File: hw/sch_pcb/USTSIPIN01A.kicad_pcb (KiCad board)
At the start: 2 copper layers, 90.9 x 50.3 mm, 112 parts, among them J1 HEADER_2x01_PARALLEL, J19 HEADER_2x01_PARALLEL, J2 HEADER_2x01_PARALLEL, J22 HEADER_2x03, J3 HEADER_2x01_PARALLEL, J4 HEADER_1x01, J5 HEADER_1x01, J6 HEADER_1x01, J7 HEADER_1x01, M1 HOLE, M2 HOLE, M3 HOLE, M4 HOLE, M5 BMI-S-210-F, M6 BMI-S-210-F, M7 BMI-S-210-F, M8 BMI-S-204-F, U1 OPA2314, U10 ATMEGA1284P-AU, U11 PCF85263A, U2 OPA2314, U3 ISL21080DIH312Z-TK 1V25, U4 TS7211, U5 TS5A4594, U6 TPS613221ADBV, U8 TPS613222ADBV, Y1 16MHz, Y2 ABS07-120-32.768KHZ-T

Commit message: Edit schema
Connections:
- C24 pad 1: /K -> /Ubiasout
- R22 pad 1: /K -> /Ubiasout
- U10 pad 11: (no net) -> unconnected-(U10-Pad11)
- U10 pad 12: (no net) -> unconnected-(U10-Pad12)
- U10 pad 13: (no net) -> unconnected-(U10-Pad13)
- U10 pad 14: (no net) -> unconnected-(U10-Pad14)
- U10 pad 15: (no net) -> unconnected-(U10-Pad15)
- U10 pad 16: (no net) -> unconnected-(U10-Pad16)
- U10 pad 21: (no net) -> unconnected-(U10-Pad21)
- U10 pad 23: (no net) -> unconnected-(U10-Pad23)
- U10 pad 24: (no net) -> unconnected-(U10-Pad24)
- U10 pad 25: (no net) -> unconnected-(U10-Pad25)
- U10 pad 30: (no net) -> unconnected-(U10-Pad30)
- U10 pad 31: (no net) -> unconnected-(U10-Pad31)
- U10 pad 32: (no net) -> unconnected-(U10-Pad32)
- U10 pad 33: (no net) -> unconnected-(U10-Pad33)
- U10 pad 34: (no net) -> unconnected-(U10-Pad34)
- U10 pad 35: (no net) -> unconnected-(U10-Pad35)
- U10 pad 41: (no net) -> unconnected-(U10-Pad41)
- U10 pad 42: (no net) -> unconnected-(U10-Pad42)
- U10 pad 43: (no net) -> unconnected-(U10-Pad43)
- U10 pad 44: (no net) -> unconnected-(U10-Pad44)
- U11 pad 4: (no net) -> unconnected-(U11-Pad4)
- U11 pad 8: (no net) -> unconnected-(U11-Pad8)
- U11 pad 9: (no net) -> unconnected-(U11-Pad9)
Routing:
- net /Ubiasout: track 0.00 -> 5.94 mm
- net /K: track 5.94 -> 0.00 mm

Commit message: Edit schema
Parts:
- added C22: 10uF, Mlab_R:SMD-0805, F.Cu at (68.6, 20.3)
- added C25: 100nF, Mlab_R:SMD-0805, F.Cu at (72.8, 20.3)
- added C36: 100nF, Mlab_R:SMD-0805, F.Cu at (81.6, 12.9)
- added C37: 1uF, Mlab_R:SMD-0805, F.Cu at (34.5, 54.9)
- added C38: 10uF, Mlab_C:SMD-0805, F.Cu at (133.4, 9.87)
- added C41: 10uF, Mlab_C:SMD-0805, F.Cu at (114.5, 27.0)
- added C45: 100nF, Mlab_C:SMD-0805, F.Cu at (121.0, 20.2)
- added C46: 100nF, Mlab_C:SMD-0805, F.Cu at (106.2, 36.6)
- added C48: 100nF, Mlab_C:SMD-0805, F.Cu at (120.7, 23.0)
- added D1: BZX585-B5V6.115, Diode_SMD:D_SOD-523, F.Cu at (108.0, 26.6)
- added D3: RED, Mlab_D:LED_1206, F.Cu at (128.2, 9.77)
- added D4: GREEN, Mlab_D:LED_1206, F.Cu at (115.5, 23.7)
- added J1: SM08B-GHS-TB, Connector_JST:JST_GH_SM08B-GHS-TB_1x08-1MP_P1.25mm_Horizontal, F.Cu at (74.2, 7.81)
- added J10: HEADER_2x01_PARALLEL, Mlab_Pin_Headers:Straight_2x01, F.Cu at (109.3, 29.8)
- added J11: HEADER_2x01_PARALLEL, Mlab_Pin_Headers:Straight_2x01, F.Cu at (128.2, 5.93)
- added J12: HEADER_2x01_PARALLEL, Mlab_Pin_Headers:Straight_2x01, F.Cu at (122.0, 9.62)
- added J13: -, Mlab_Pin_Headers:Straight_2x01, F.Cu at (122.0, 17.0)
- added J14: -, Mlab_Pin_Headers:Straight_2x01, F.Cu at (103.1, 29.8)
- added J15: -, Mlab_Pin_Headers:Straight_2x01, F.Cu at (103.1, 33.5)
- added J16: -, Mlab_Pin_Headers:Straight_2x01, F.Cu at (109.3, 23.5)
- added J17: HEADER_2x01_PARALLEL, Mlab_Pin_Headers:Straight_2x01, F.Cu at (122.0, 13.3)
- added J18: -, Mlab_Pin_Headers:Straight_1x01, F.Cu at (118.4, 27.5)
- added J2: SD_Card-FPS009-4200-0, Mlab_CON:FPS009-4200-0, F.Cu at (65.7, 24.6)
- added J20: -, Mlab_Pin_Headers:Straight_1x01, F.Cu at (124.9, 20.7)
- added J21: -, Mlab_Pin_Headers:Straight_1x01, F.Cu at (112.2, 33.5)
- added J23: -, Mlab_Pin_Headers:Straight_1x01, F.Cu at (131.1, 13.6)
- added J3: SM06B-GHS-TB, Connector_JST:JST_GH_SM06B-GHS-TB_1x06-1MP_P1.25mm_Horizontal, F.Cu at (73.0, 15.3)
- added J4: HEADER_1x01, Mlab_Pin_Headers:Straight_1x01, F.Cu at (68.3, 23.5)
- added J5: HEADER_1x01, Mlab_Pin_Headers:Straight_1x01, F.Cu at (46.3, 43.4)
- added J6: HEADER_1x01, Mlab_Pin_Headers:Straight_1x01, F.Cu at (50.0, 43.4)
- added J7: HEADER_1x01, Mlab_Pin_Headers:Straight_1x01, F.Cu at (42.6, 43.4)
- added J8: USB_B, Connector_USB:USB_B_OST_USB-B1HSxx_Horizontal, F.Cu at (102.8, 11.6)
- added J9: HEADER_2x01_PARALLEL, Mlab_Pin_Headers:Straight_2x01, F.Cu at (122.0, 5.93)
- added L2: L, Mlab_R:SMD-0805, F.Cu at (30.3, 45.6)
- added Q1: BF862, Mlab_T:SOT-23, F.Cu at (30.1, 53.0)
- added R14: 4k7, Mlab_R:SMD-0805, F.Cu at (34.1, 52.2)
- added R16: 4k7, Mlab_R:SMD-0805, F.Cu at (30.3, 56.4)
- added R17: 100, Mlab_R:SMD-0805, F.Cu at (34.5, 45.6)
- added R18: 100, Mlab_R:SMD-0805, F.Cu at (38.7, 42.9)
- added R24: 100, Mlab_R:SMD-0805, F.Cu at (34.5, 42.9)
- added R25: 100, Mlab_R:SMD-0805, F.Cu at (30.3, 42.9)
- added R26: 4k7, Mlab_R:SMD-0805, F.Cu at (108.3, 33.0)
- added R27: 10k, Mlab_R:SMD-0805, F.Cu at (127.2, 15.8)
- added R28: 270R, Mlab_R:SMD-0805, F.Cu at (127.2, 13.1)
- added R29: 270R, Mlab_R:SMD-0805, F.Cu at (102.0, 36.6)
- added U6: AT24CS64-SSHM, Package_SO:SOIC-8_3.9x4.9mm_P1.27mm, F.Cu at (86.2, 7.31)
- added U7: USBLC6-2SC6, Package_TO_SOT_SMD:SOT-23-6, F.Cu at (133.9, 6.31)
- added U9: FT231XQ, Package_DFN_QFN:QFN-20-1EP_4x4mm_P0.5mm_EP2.5x2.5mm, F.Cu at (103.1, 24.8)
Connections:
- C1 pad 1: +3V3 -> POWER_ANALOG_3V3
- C32 pad 1: VDD -> POWER_ANALOG_3V3
- C4 pad 1: +3V3 -> POWER_ANALOG_3V3
- F2 pad 2: /power/3 -> UAV_5V
- L3 pad 1: VDD -> POWER_ANALOG_3V3
- R2 pad 2: +3V3 -> POWER_ANALOG_3V3
- R3 pad 2: +3V3 -> POWER_ANALOG_3V3
- R4 pad 2: +3V3 -> POWER_ANALOG_3V3
- R5 pad 2: +3V3 -> POWER_ANALOG_3V3
- U10 pad 11: unconnected-(U10-Pad11) -> /cpu/RX1
- U10 pad 12: unconnected-(U10-Pad12) -> /cpu/TX1
- U10 pad 13: unconnected-(U10-Pad13) -> /cpu/TIMEPULSE
- U10 pad 14: unconnected-(U10-Pad14) -> /cpu/EXTINT
- U10 pad 15: unconnected-(U10-Pad15) -> /cpu/GEO_STAT
- U10 pad 16: unconnected-(U10-Pad16) -> POWER_ANALOG_3V3
- U10 pad 23: unconnected-(U10-Pad23) -> /cpu/PC4
- U10 pad 26: /cpu/PC7 -> unconnected-(U10-Pad26)
- U10 pad 41: unconnected-(U10-Pad41) -> Net-(L2-Pad1)
- U10 pad 42: unconnected-(U10-Pad42) -> Net-(L2-Pad1)
- U10 pad 43: unconnected-(U10-Pad43) -> Net-(L2-Pad1)
- U10 pad 44: unconnected-(U10-Pad44) -> /cpu/PB4
- U3 pad 1: +3V3 -> POWER_ANALOG_3V3
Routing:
- net unconnected-(U10-Pad26): track 0.00 -> 20.3 mm
- net /cpu/PC7: track 20.3 -> 0.00 mm

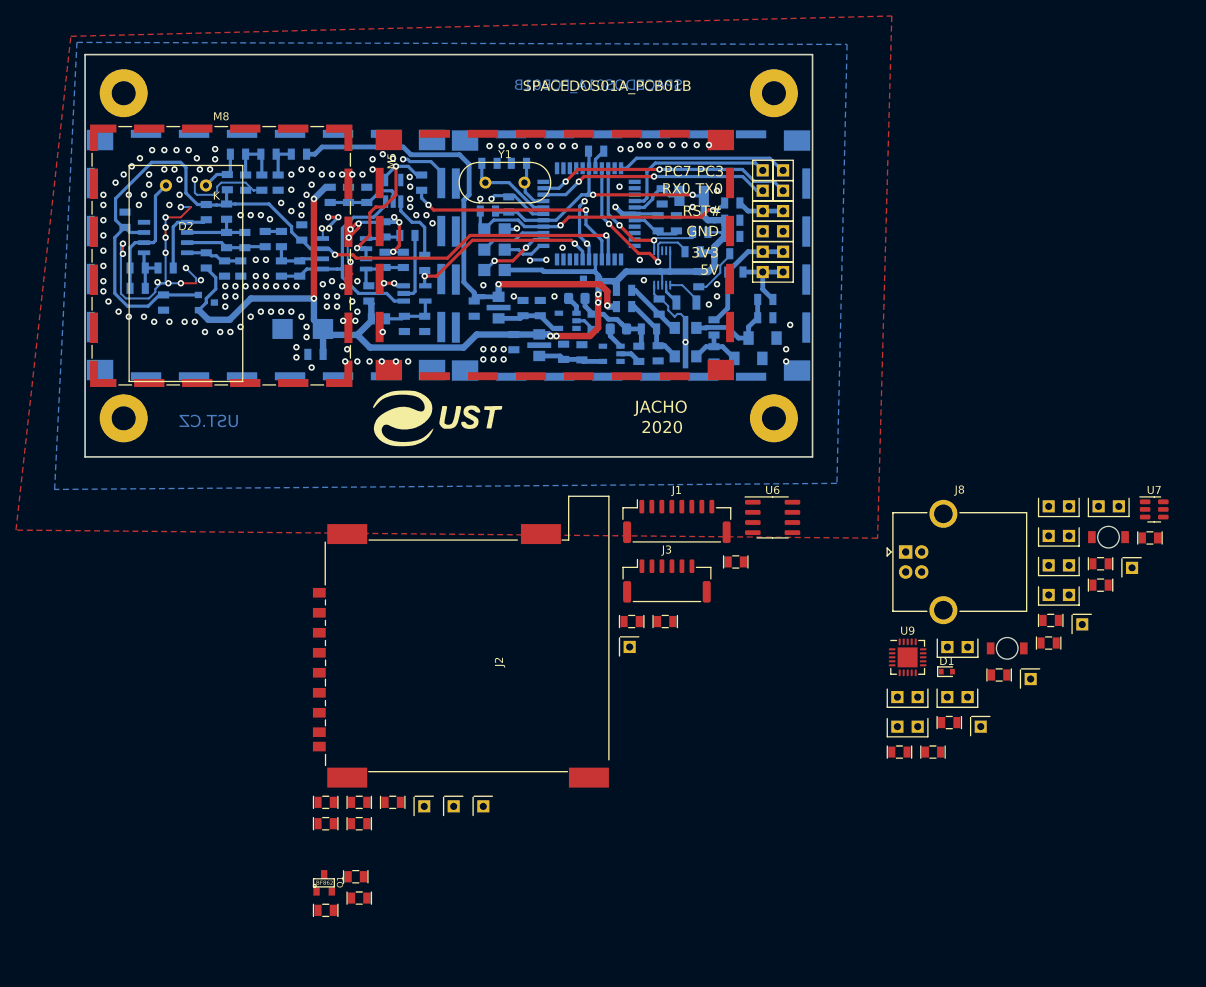
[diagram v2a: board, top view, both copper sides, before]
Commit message: Edit schema and PCB
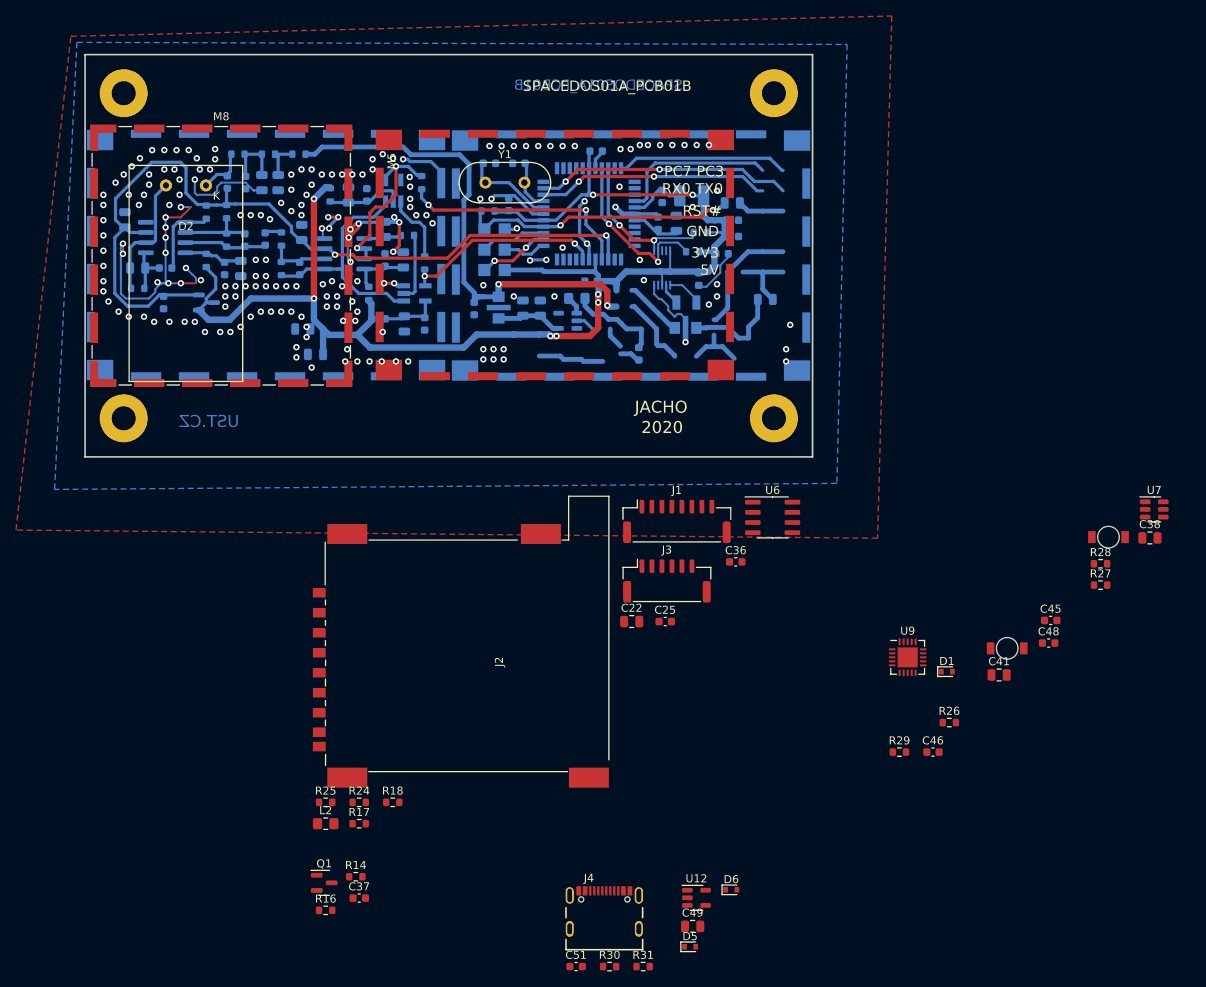
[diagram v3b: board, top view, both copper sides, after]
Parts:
- removed the C22 at (78.9, -13.1)
- removed the C25 at (63.8, -17.1)
- removed the C36 at (85.3, -17.7)
- removed the C38 at (60.1, -13.4)
- removed the C45 at (75.3, -12.8)
- removed the C48 at (71.9, -13.2)
- removed C53, C55: 100nF, Mlab_R:SMD-0805
- removed the D1 at (83.2, -12.6)
- removed the D3 at (84.9, -15.1)
- removed F1: SR010-15 100mA, Mlab_R:SMD-0805
- removed G***: LOGO, MLAB_LOGA:UST
- removed the J1 at (86.2, -25.9)
- removed J10, J11, J12, J17, J19, J9: HEADER_2x01_PARALLEL, Mlab_Pin_Headers:Straight_2x01
- removed J13, J14, J15, J16: -, Mlab_Pin_Headers:Straight_2x01
- removed J18, J20, J21, J23: -, Mlab_Pin_Headers:Straight_1x01
- removed the J2 at (86.2, -28.4)
- removed the J3 at (86.2, -23.4)
- removed the J4 at (85.0, -36.1)
- removed the J4 at (68.3, 23.5)
- removed J5 (x2), J6 (x2), J7 (x2): HEADER_1x01, Mlab_Pin_Headers:Straight_1x01
- removed J8: USB_B, Connector_USB:USB_B_OST_USB-B1HSxx_Horizontal
- removed the L2 at (66.9, -16.3)
- removed the R24 at (81.5, -23.4)
- removed the R25 at (67.6, -19.1)
- removed the R27 at (67.6, -21.1)
- removed the R28 at (70.7, -16.3)
- removed the U6 at (66.1, -13.1)
- added D5: BZX585-B5V6.115, Diode_SMD:D_SOD-523, F.Cu at (75.9, 61.0)
- added D6: BZX585-B5V6.115, Diode_SMD:D_SOD-523, F.Cu at (81.0, 53.9)
- added J4: USBC_USB4105-GF-A, Mlab_CON:USBC GCT_USB4105-GF-A, F.Cu at (65.2, 58.7)
- added R30: 5k1, Resistor_SMD:R_0603_1608Metric, F.Cu at (65.8, 63.5)
- added R31: 5k1, Resistor_SMD:R_0603_1608Metric, F.Cu at (70.0, 63.5)
- added U12: MIC5504-3.3YM5, Package_TO_SOT_SMD:SOT-23-5, F.Cu at (76.7, 54.9)
- C1: value 47uF -> 47uF/6V3; footprint Mlab_C:TantalC_SizeC_Reflow -> Capacitor_SMD:C_0805_2012Metric
- C10, C11, C12, C13, C14, C15, C16, C18, C2, C20, C24, C25, C26, C27, C28, C30, C31, C32, C33, C34, C35, C36, C37, C39, C44, C47, C54: footprint Mlab_R:SMD-0805 -> Capacitor_SMD:C_0603_1608Metric
- C17, C19, C21, C22, C23, C3, C4, C40, C42, C43, C5, C50, C6, C7, C8, C9: footprint Mlab_R:SMD-0805 -> Capacitor_SMD:C_0805_2012Metric
- C38, C41: footprint Mlab_C:SMD-0805 -> Capacitor_SMD:C_0805_2012Metric
- C45, C46, C48: footprint Mlab_C:SMD-0805 -> Capacitor_SMD:C_0603_1608Metric
- C49: footprint Mlab_R:SMD-0805 -> Capacitor_SMD:C_0805_2012Metric; moved to F.Cu
- C51: value NFM21PC105-1uF -> 100nF; footprint Mlab_L:FIR_0805 -> Capacitor_SMD:C_0603_1608Metric; moved to F.Cu
- F2: footprint Mlab_R:SMD-0805 -> Fuse:Fuse_0805_2012Metric
- L1: footprint Mlab_R:SMD-1210 -> Inductor_SMD:L_1210_3225Metric_Pad1.42x2.65mm_HandSolder
- L2: value L -> 100uH; footprint Mlab_R:SMD-0805 -> Inductor_SMD:L_0805_2012Metric_Pad1.15x1.40mm_HandSolder
- L3: footprint Resistor_SMD:R_0805_2012Metric_Pad1.15x1.40mm_HandSolder -> Inductor_SMD:L_0805_2012Metric_Pad1.15x1.40mm_HandSolder
- Q1: footprint Mlab_T:SOT-23 -> Package_TO_SOT_SMD:SOT-23
- R1, R10, R11, R12, R13, R14, R15, R16, R17, R18, R19, R2, R20, R21, R22, R23, R24, R25, R26, R27, R28, R29, R3, R4, R5, R6, R7, R8, R9: footprint Mlab_R:SMD-0805 -> Resistor_SMD:R_0603_1608Metric
- U1, U2: footprint Mlab_IO:SOIC-8_3.9x4.9mm_Pitch1.27mm -> Package_SO:SOIC-8_3.9x4.9mm_P1.27mm
- U11: footprint Mlab_IO:TSSOP-10_3x3mm_Pitch0.5mm -> Package_SO:TSSOP-10_3x3mm_P0.5mm
- moved C51 77.8 mm to (61.6, 63.5), turned to 0 degrees
- moved C49 73.1 mm to (76.2, 58.4), turned to 0 degrees
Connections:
- C43 pad 2: /cpu/RST# -> RST#
- C48 pad 1: GND -> +3V3
- C48 pad 2: +3V3 -> GND
- C49 pad 1: Net-(C38-Pad1) -> +3V3
- C51 pad 1: Net-(C38-Pad1) -> +3V3
- F2 pad 2: UAV_5V -> Net-(F2-Pad2)
- J3 pad 2: /cpu/RX0 -> RX0
- J3 pad 3: /cpu/TX0 -> TX0
- R26 pad 1: Net-(C29-Pad3) -> /power/VBUS
- U10 pad 10: /cpu/TX0 -> TX0
- U10 pad 9: /cpu/RX0 -> RX0
- U7 pad 5: UAV_5V -> /power/VBUS
- U9 pad 1: /power/RXD -> TX0
- U9 pad 12: Net-(C29-Pad3) -> +3V3
- U9 pad 15: /power/CBUS0 -> unconnected-(U9-Pad15)
- U9 pad 16: /power/CBUS3 -> unconnected-(U9-Pad16)
- U9 pad 17: /power/TXD -> RX0
- U9 pad 18: /power/#DTR -> unconnected-(U9-Pad18)
- U9 pad 19: /power/#RTS -> RST#
- U9 pad 2: /power/#RI -> unconnected-(U9-Pad2)
- U9 pad 4: /power/#DSR -> unconnected-(U9-Pad4)
- U9 pad 5: /power/#DCD -> unconnected-(U9-Pad5)
- U9 pad 6: /power/#CTS -> unconnected-(U9-Pad6)
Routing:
- net (no net): track 0.00 -> 42.2 mm
- net TX0: track 0.00 -> 32.0 mm, vias 0 -> 2
- net /cpu/TX0: track 32.0 -> 0.00 mm, vias 2 -> 0
- net RX0: track 0.00 -> 29.1 mm, vias 0 -> 2
- net /cpu/RX0: track 29.1 -> 0.00 mm, vias 2 -> 0
- net /power/5: track 14.8 -> 0.00 mm
- net VDD: track 11.5 -> 0.00 mm
- net POWER_ANALOG_3V3: track 0.00 -> 11.5 mm
- net Net-(C45-Pad3): track 9.12 -> 0.00 mm
- net Net-(F2-Pad2): track 0.00 -> 8.97 mm
- net /power/3: track 8.97 -> 0.00 mm
- net Net-(C38-Pad1): track 8.24 -> 0.00 mm
- net Net-(C22-Pad1): track 7.31 -> 0.00 mm
- net RST#: track 0.00 -> 5.82 mm
- net /cpu/RST#: track 5.82 -> 0.00 mm
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
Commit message: Edit schema and PCB
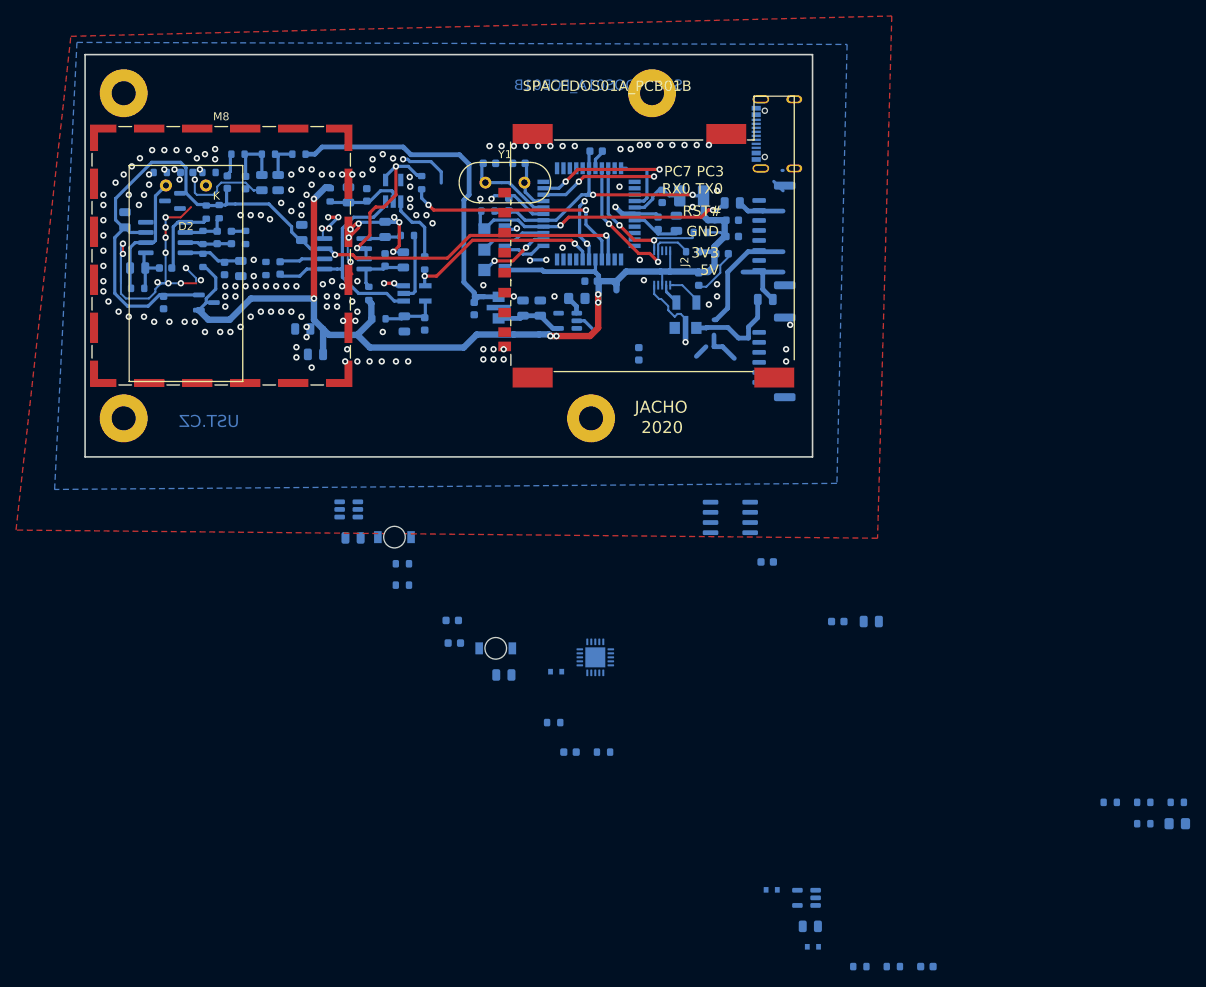
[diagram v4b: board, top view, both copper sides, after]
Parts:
- removed M5, M6, M7: BMI-S-210-F, Mlab_Mechanical:BMI-S-210-F
- C22, C25, C36, C37, C38, C41, C45, C46, C48, C49, C51, D1, D3, D4, D5, D6, J1, J3, J4, L2, Q1, R14, R16, R17, R18, R24, R25, R26, R27, R28, R29, R30, R31, U12, U6, U7, U9: moved to B.Cu
- moved L2 106.4 mm to (136.8, 45.6), turned to 180 degrees
- moved R25 106.4 mm to (136.8, 42.9), turned to 180 degrees
- moved J4 102.2 mm to (88.9, -40.6), turned to -90 degrees
- moved U7 100.7 mm to (33.2, 6.31), turned to 180 degrees
- moved C38 99.6 mm to (33.7, 9.87), turned to 180 degrees
- moved R17 98.1 mm to (132.6, 45.6), turned to 180 degrees
- moved R24 98.1 mm to (132.6, 42.9), turned to 180 degrees
- moved R16 93.4 mm to (15.7, -35.8)
- moved C37 93.2 mm to (13.0, -35.8)
- moved R14 91.4 mm to (9.65, -35.8), turned to 180 degrees
- moved R18 89.7 mm to (128.4, 42.9), turned to 180 degrees
- moved D3 89.3 mm to (38.9, 9.77), turned to 180 degrees
- moved Q1 87.3 mm to (11.2, -32.3), turned to 180 degrees
- moved R27 87.3 mm to (39.9, 15.8), turned to 180 degrees
- moved R28 87.3 mm to (39.9, 13.1), turned to 180 degrees
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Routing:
- net (no net): track 42.2 -> 6.31 mm
- net /cpu/PC3: track 21.4 -> 0.80 mm
- net +5V: track 62.5 -> 44.0 mm, vias 2 -> 0
- net TX0: track 32.0 -> 15.5 mm
- net unconnected-(U10-Pad26): track 20.3 -> 5.01 mm
- net /cpu/TX1: track 0.00 -> 14.8 mm
- net RX0: track 29.1 -> 14.8 mm
- net POWER_ANALOG_3V3: track 11.5 -> 0.00 mm
- net Net-(C29-Pad3): track 7.33 -> 0.24 mm
- net Net-(C15-Pad1): track 10.1 -> 5.84 mm
- net /Ubiasout: track 5.94 -> 2.70 mm
- net Net-(C15-Pad2): track 8.86 -> 5.81 mm
- net GND: track 133.6 -> 131.3 mm, vias 189 -> 180
- net Net-(C18-Pad2): track 7.06 -> 5.28 mm
- net unconnected-(J2-Pad8): vias 0 -> 1
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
